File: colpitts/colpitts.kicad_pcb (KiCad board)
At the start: 2 copper layers, 37 parts, among them J101 BORNERA, J102 BNC, Q101 2N3904, Q102 2N3904, Q103 2N3904, Q104 2N3904, U101 LM741

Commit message: Lectura de netlist, def área pcb, board setup
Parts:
- added FID101: Fiducial, Fiducial:Fiducial_1mm_Mask2mm, F.Cu at (153.1, 24.1)
- added FID102: Fiducial, Fiducial:Fiducial_1mm_Mask2mm, F.Cu at (152.7, 48.1)
- added FID103: Fiducial, Fiducial:Fiducial_1mm_Mask2mm, F.Cu at (162.1, 40.1)
- added FID104: Fiducial, Fiducial:Fiducial_1mm_Mask2mm, F.Cu at (149.1, 54.4)
- added FID105: Fiducial, Fiducial:Fiducial_1mm_Mask2mm, F.Cu at (157.5, 45.1)
- added FID106: Fiducial, Fiducial:Fiducial_1mm_Mask2mm, F.Cu at (166.9, 35.0)
- added H101: MountingHole, MountingHole:MountingHole_3.2mm_M3_Pad_Via, F.Cu at (147.3, 26.4)
- added H102: MountingHole, MountingHole:MountingHole_3.2mm_M3_Pad_Via, F.Cu at (159.5, 22.6)
- added H103: MountingHole, MountingHole:MountingHole_3.2mm_M3_Pad_Via, F.Cu at (137.5, 43.5)
- added H104: MountingHole, MountingHole:MountingHole_3.2mm_M3_Pad_Via, F.Cu at (155.3, 30.6)
- moved C106 82.0 mm to (152.2, 36.0)
- moved C115 73.5 mm to (153.2, 39.0)
- moved C113 72.3 mm to (158.0, 41.9)
- moved Q101 70.2 mm to (165.5, 21.9)
- moved C114 69.0 mm to (161.6, 31.0)
- moved C107 67.1 mm to (148.5, 40.5)
- moved R101 61.8 mm to (141.9, 51.1)
- moved Q102 60.4 mm to (145.3, 33.6)
- moved C103 58.5 mm to (162.7, 36.9)
- moved C108 58.0 mm to (161.6, 28.1)
- moved R104 57.9 mm to (148.6, 46.4)
- moved R105 57.6 mm to (166.4, 25.9)
- moved C102 55.4 mm to (166.5, 31.8)
- moved C110 51.7 mm to (143.8, 48.2)
- moved Q103 51.1 mm to (135.1, 50.7)
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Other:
- board outline added: 70 x 50 mm
- rule trace_min: 0.2 -> 0.25
- rule via_min_drill: 0.3 -> 0.4
- rule via_min_size: 0.4 -> 0.8
- board text added: "Reference technology: 8 mils Size: 70 x 50 mm Thinner track: 0.25 mm Min hole size: 0.4 mm Min track spacing: 0.25 mm Distance to pcb edge: 0.3 mm STACK-UP FR4 Dual layer PCB thickness: 1.6 mm Copper thickness: 1 Oz (35 um) Components only on top layer Mask color (preferably): blue Silkscreen color: white Termitation: HASL w/Pb No special requirements"

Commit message: Pos componentes, ruteo, rellenos
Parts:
- FID104, FID105, FID106: moved to B.Cu
- moved FID101 98.2 mm to (99.8, 106.7)
- moved FID106 98.1 mm to (99.8, 106.7)
- moved H101 95.9 mm to (94.0, 106.0)
- moved R105 95.0 mm to (101.0, 94.7)
- moved C102 93.9 mm to (93.0, 90.2), turned to 270 degrees
- moved C104 93.7 mm to (95.5, 90.2), turned to 270 degrees
- moved Q101 93.3 mm to (113.9, 99.7), turned to 90 degrees
- moved H102 83.5 mm to (155.0, 106.0)
- moved C103 82.9 mm to (95.5, 85.3), turned to 270 degrees
- moved C108 81.7 mm to (112.0, 93.0), turned to 270 degrees
- moved C101 80.8 mm to (93.0, 85.3), turned to 270 degrees
- moved L101 79.0 mm to (93.0, 81.0)
- moved C106 76.6 mm to (98.0, 90.2), turned to 270 degrees
- moved R104 69.7 mm to (101.0, 97.3), turned to 180 degrees
- moved Q102 68.0 mm to (107.6, 90.2), turned to 90 degrees
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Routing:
- net -15V: track 0.00 -> 92.4 mm, vias 0 -> 1
- net +15V: track 0.00 -> 80.5 mm, vias 0 -> 1
- net GND: track 0.00 -> 67.3 mm, vias 0 -> 11
- net /Vcontrol: track 0.00 -> 47.0 mm
- net Net-(C107-Pad1): track 0.00 -> 23.5 mm
- net Net-(RV101-Pad2): track 0.00 -> 22.1 mm
- net Net-(C102-Pad1): track 0.00 -> 17.5 mm
- net Net-(C113-Pad2): track 0.00 -> 16.5 mm
- net /Vout: track 0.00 -> 14.7 mm
- net Net-(C114-Pad2): track 0.00 -> 13.9 mm
- net Net-(Q101-Pad1): track 0.00 -> 12.9 mm
- net Net-(C107-Pad2): track 0.00 -> 12.6 mm
- net Net-(Q101-Pad2): track 0.00 -> 11.8 mm
- net Net-(JP102-Pad2): track 0.00 -> 10.6 mm
- net Net-(Q103-Pad1): track 0.00 -> 7.12 mm
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- added copper zone on B.Cu, net GND
- added copper zone on F.Cu, net GND
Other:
- board size 70 x 50 mm -> 69 x 40 mm
- board text added: "Reference technology: 8 mils Size: 80 x 50 mm Thinner track: 0.25 mm Min hole size: 0.4 mm Min track spacing: 0.25 mm Distance to pcb edge: 0.3 mm STACK-UP FR4 Dual layer PCB thickness: 1.6 mm Copper thickness: 1 Oz (35 um) Components only on top layer Mask color (preferably): blue Silkscreen color: white Termitation: HASL w/Pb No special requirements"
- board text removed: "Reference technology: 8 mils Size: 70 x 50 mm Thinner track: 0.25 mm Min hole size: 0.4 mm Min track spacing: 0.25 mm Distance to pcb edge: 0.3 mm STACK-UP FR4 Dual layer PCB thickness: 1.6 mm Copper thickness: 1 Oz (35 um) Components only on top layer Mask color (preferably): blue Silkscreen color: white Termitation: HASL w/Pb No special requirements"

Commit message: Terminación rellenos
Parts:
- moved H102 1.00 mm to (156.0, 106.0)
- moved H104 1.00 mm to (156.0, 74.0)
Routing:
- net GND: track 67.3 -> 68.7 mm
- net Net-(C114-Pad2): track 13.9 -> 15.0 mm
- net Net-(C114-Pad1): track 3.14 -> 3.97 mm
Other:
- board size 69 x 40 mm -> 70 x 40 mm
- board text added: "Reference technology: 8 mils Size: 70 x 40 mm Thinner track: 0.25 mm Min hole size: 0.4 mm Min track spacing: 0.25 mm Distance to pcb edge: 0.3 mm STACK-UP FR4 Dual layer PCB thickness: 1.6 mm Copper thickness: 1 Oz (35 um) Components only on top layer Mask color (preferably): blue Silkscreen color: white Termitation: HASL w/Pb No special requirements"
- board text removed: "Reference technology: 8 mils Size: 80 x 50 mm Thinner track: 0.25 mm Min hole size: 0.4 mm Min track spacing: 0.25 mm Distance to pcb edge: 0.3 mm STACK-UP FR4 Dual layer PCB thickness: 1.6 mm Copper thickness: 1 Oz (35 um) Components only on top layer Mask color (preferably): blue Silkscreen color: white Termitation: HASL w/Pb No special requirements"

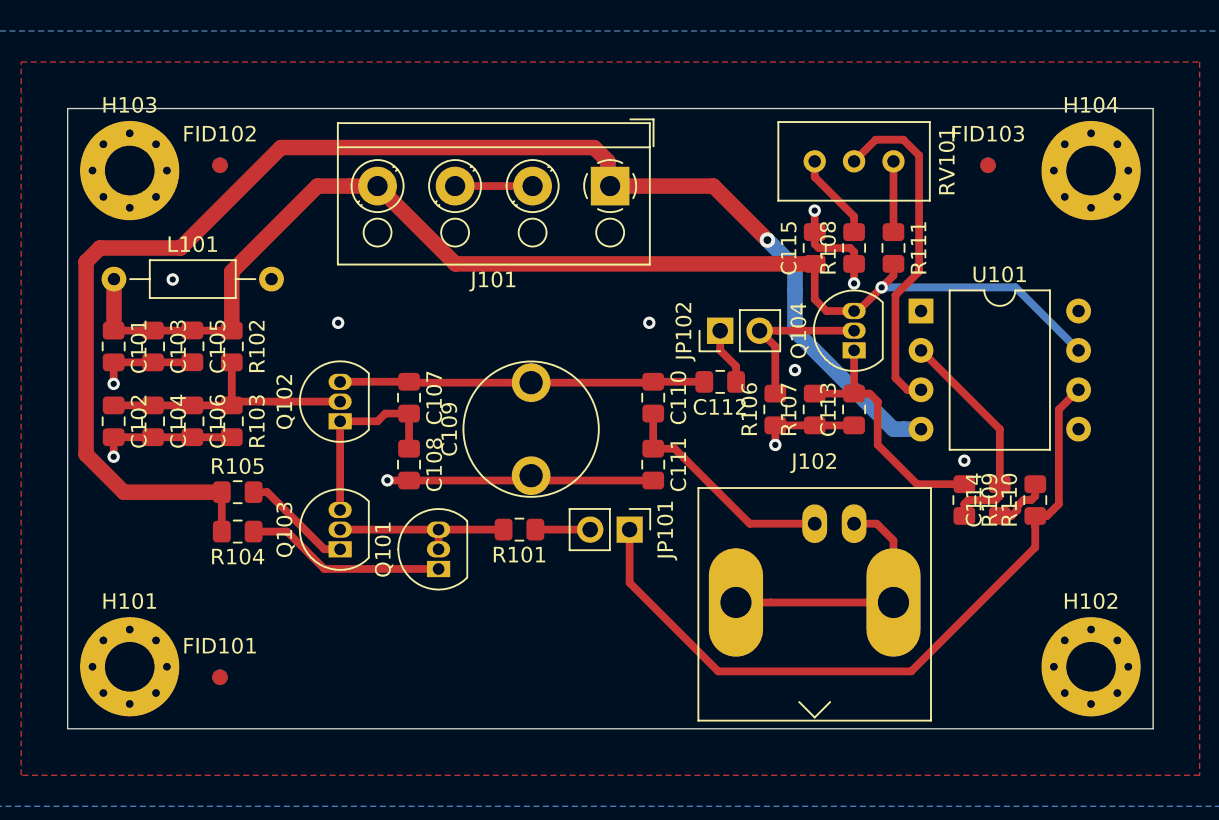
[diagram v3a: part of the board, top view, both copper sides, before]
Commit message: Anotación ref user, DRC, validación serigrafía
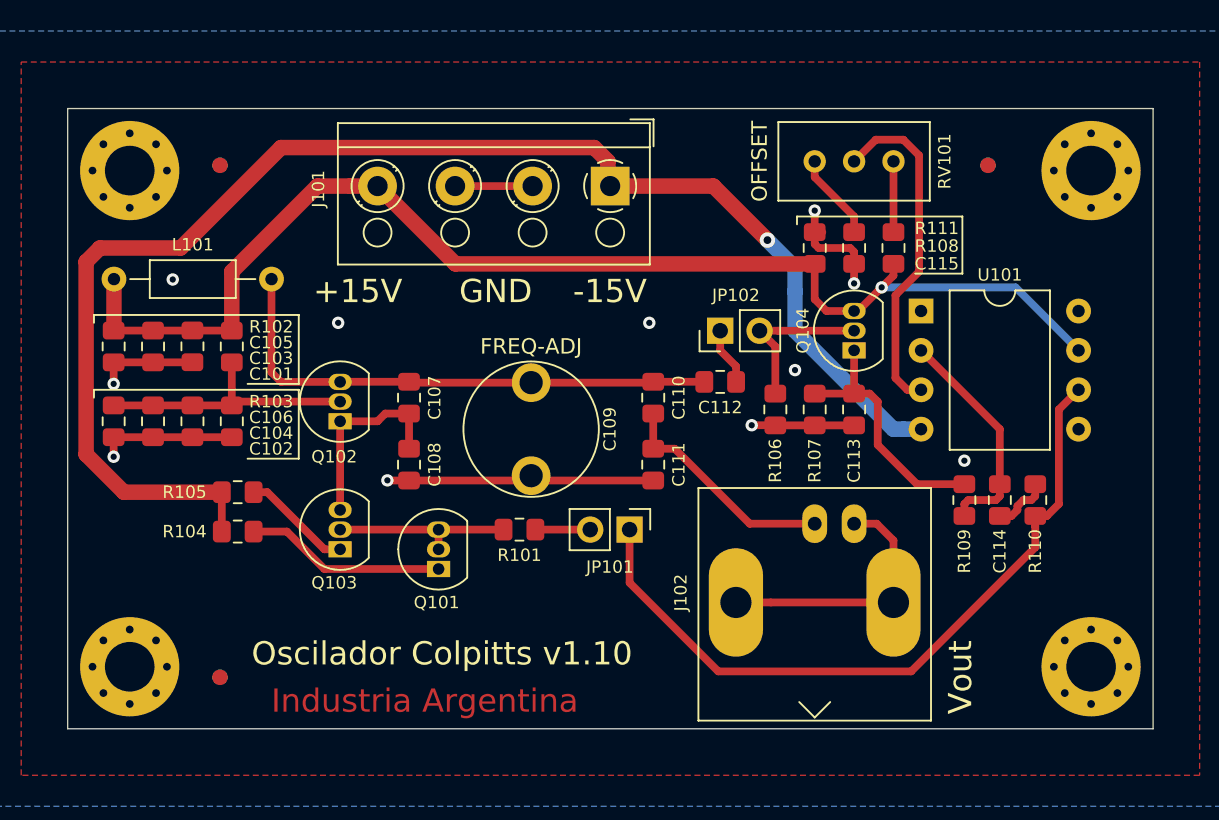
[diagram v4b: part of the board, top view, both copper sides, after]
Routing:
- net Net-(C107-Pad1): track 23.5 -> 34.2 mm
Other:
- board text added: "+15V"
- board text added: "-15V"
- board text added: "FREQ-ADJ"
- board text added: "GND"
- board text added: "Industria Argentina"
- board text added: "OFFSET"
- board text added: "Oscilador Colpitts v1.10"
- board text added: "Vout"
